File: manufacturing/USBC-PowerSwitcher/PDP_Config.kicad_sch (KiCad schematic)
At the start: 8 parts

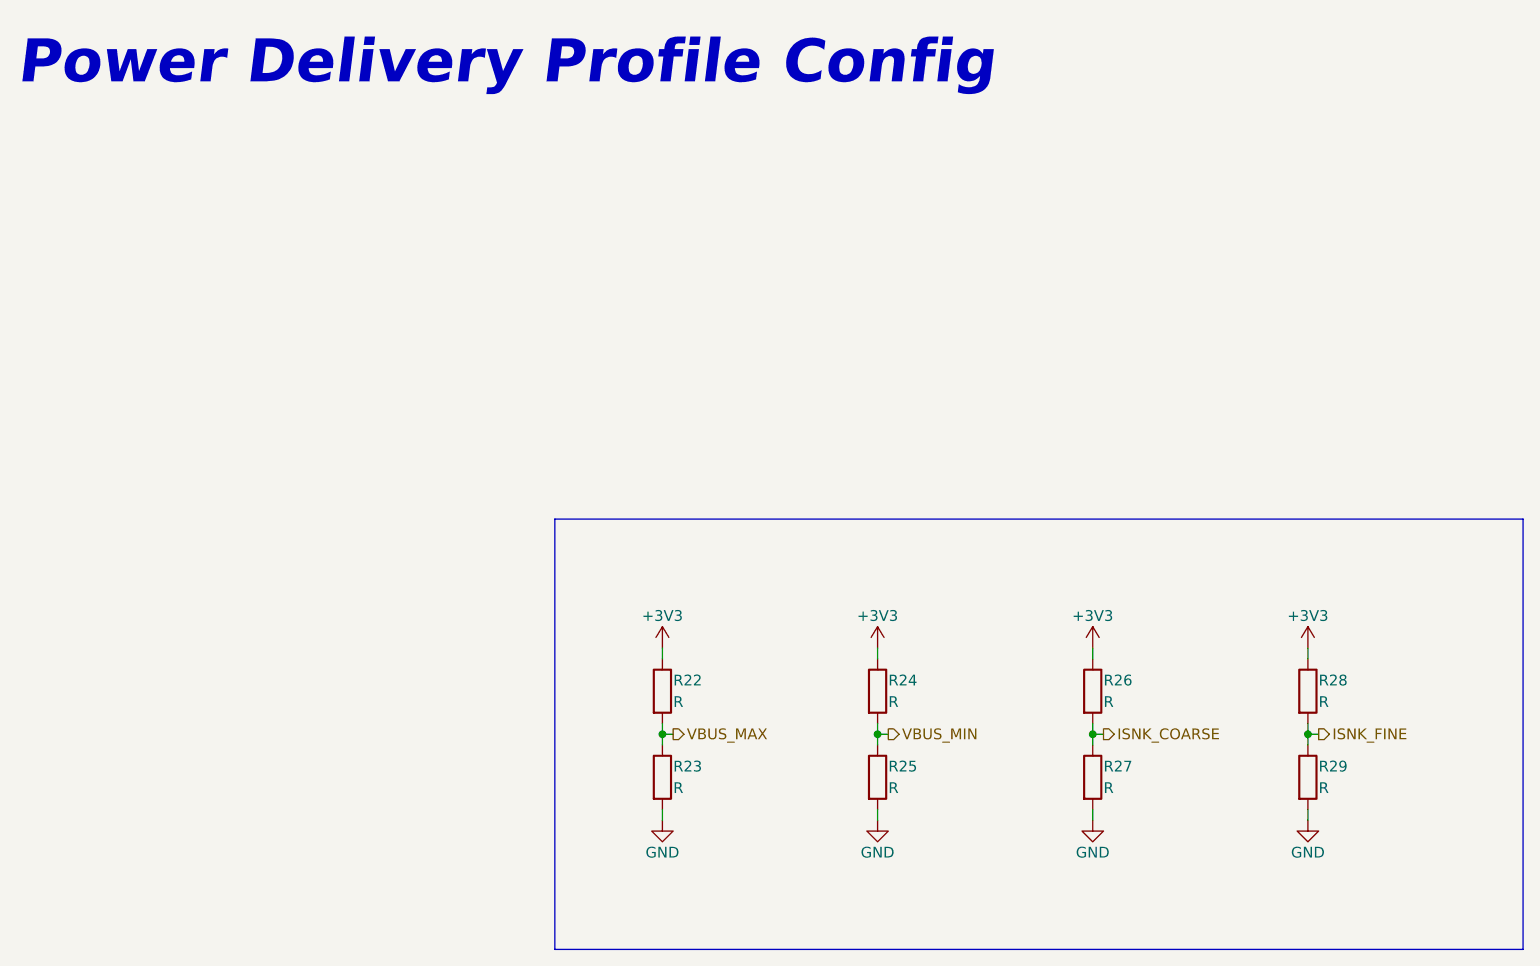
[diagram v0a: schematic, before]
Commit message: First Rough placement
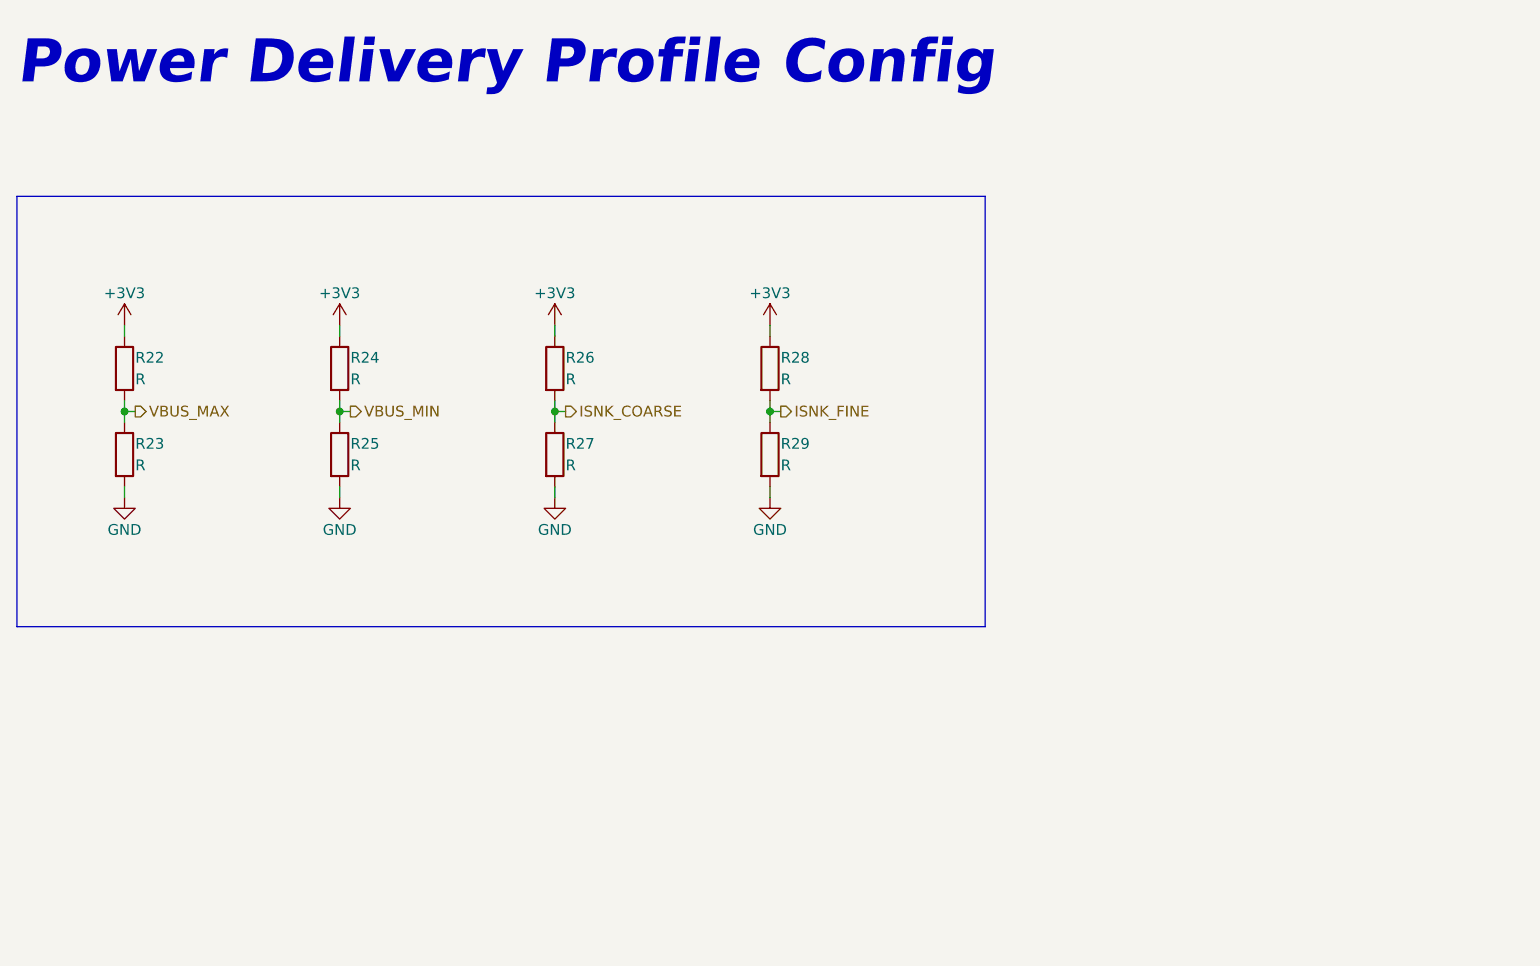
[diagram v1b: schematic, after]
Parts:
- R22, R23, R24, R25, R26, R27, R28, R29: footprint (none) -> Resistor_SMD:R_0402_1005Metric
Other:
- moved on the sheet: R22, R23, R24, R25, R26, R27, R28, R29
